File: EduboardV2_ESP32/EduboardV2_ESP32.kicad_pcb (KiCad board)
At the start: 4 copper layers, 30 x 50.9 mm, 82 parts, among them J1 EduboardV2 PCIE UP Board Conn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, Q1 S8050_C139514, Q2 S8050_C139514, Q3 AO3401A, SW1 K2-1102SP-C4SC-04, SW2 K2-1102SP-C4SC-04, U1 ESP32-WROOM-E, U2 FT2232HL, U3 M93C46-WMN6TP, U4 SX1509BIULTRT, U5 LD1117S33TR_SOT223, Y2 12MHz

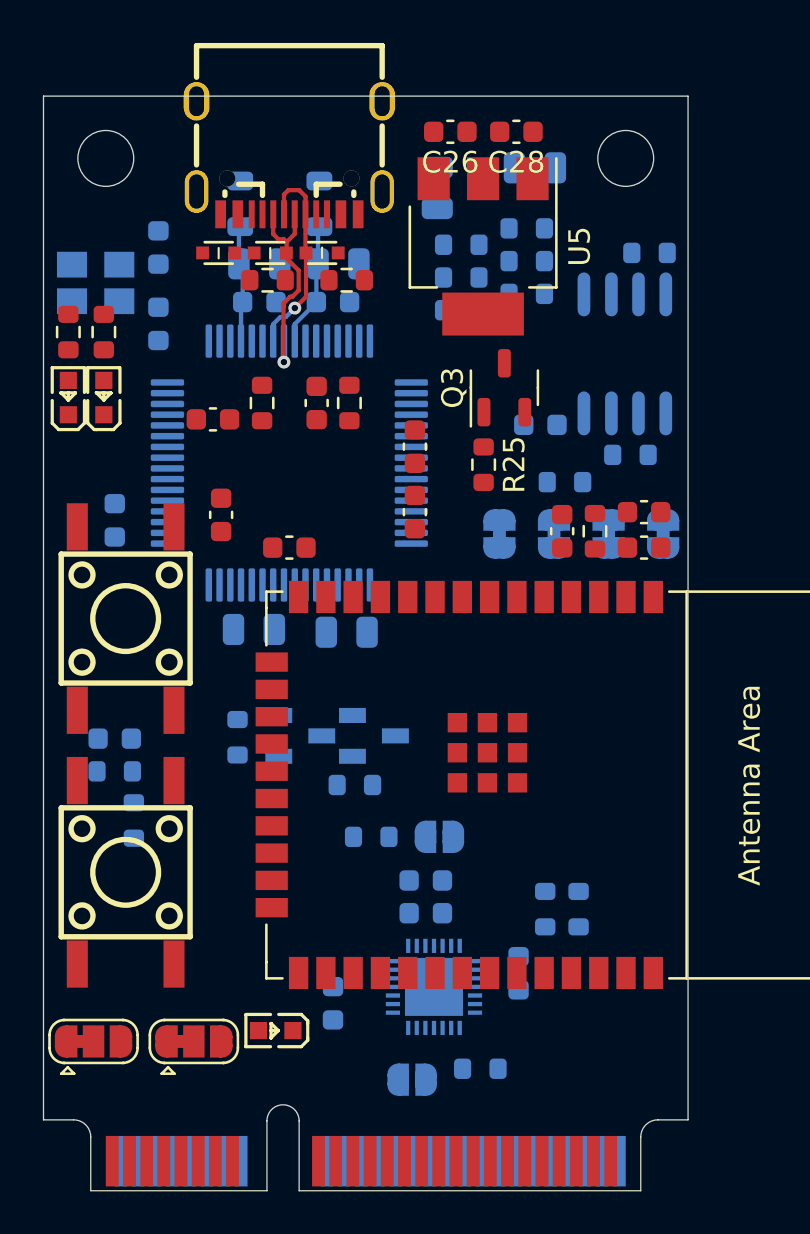
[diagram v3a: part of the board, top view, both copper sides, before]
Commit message: rework pin assignement with esp32 pin restrictions in mind. start layout
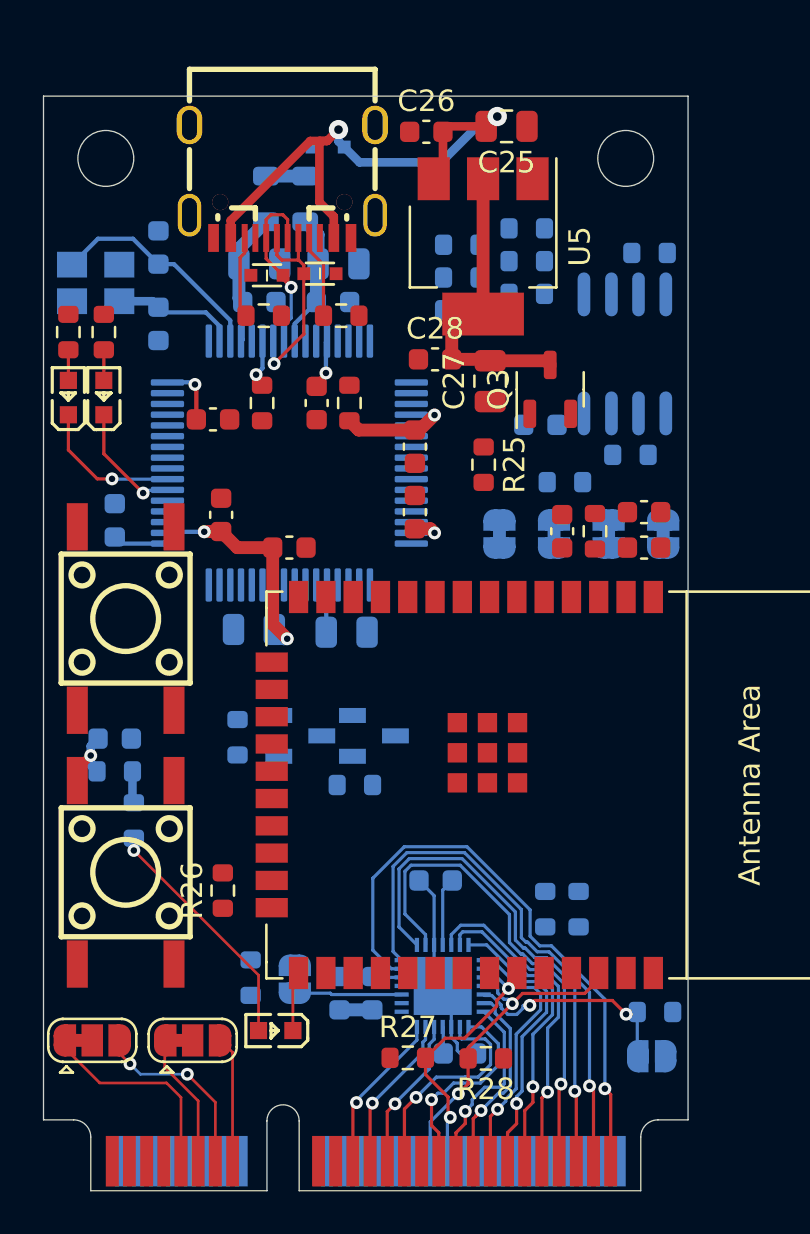
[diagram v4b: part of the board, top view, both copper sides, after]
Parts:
- added R26: 10k, Resistor_SMD:R_0603_1608Metric, F.Cu at (112.7, 143.5)
- added R27: 10k, Resistor_SMD:R_0603_1608Metric, F.Cu at (121.3, 151.3)
- added R28: 10k, Resistor_SMD:R_0603_1608Metric, F.Cu at (125.0, 151.3)
- C25, C27: moved to F.Cu
- D1: moved to B.Cu
- moved C28 11.2 mm to (122.6, 118.7), turned to 0 degrees
- moved JP5 11.2 mm to (132.7, 151.2), turned to 0 degrees
- moved C27 10.1 mm to (125.2, 119.8), turned to 90 degrees
- moved JP6 9.45 mm to (116.1, 147.6), turned to -90 degrees
- moved R24 8.63 mm to (114.0, 147.5), turned to 90 degrees
- moved R23 8.55 mm to (132.8, 149.1)
- moved C23 7.45 mm to (122.6, 143.0), turned to 180 degrees
- moved D1 7.09 mm to (117.6, 108.9)
- moved C21 6.60 mm to (118.2, 148.2), turned to 90 degrees
- moved JP7 4.73 mm to (106.7, 150.4)
- moved C24 4.63 mm to (123.8, 151.1), turned to 0 degrees
- moved JP8 4.61 mm to (111.3, 150.4)
- moved C22 4.48 mm to (119.7, 148.2), turned to 90 degrees
- moved C25 4.32 mm to (125.9, 107.9), turned to 180 degrees
- moved Q3 2.13 mm to (128.0, 120.1)
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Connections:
- J1 pad 16: GPIO_RS485_DE -> ESP_TDI
- J1 pad 17: ESP_TMS -> ESP_IO27
- J1 pad 19: ESP_TDI -> ESP_TMS
- J1 pad 21: ESP_TCK -> GPIO_RotEnc_B
- J1 pad 23: ESP_TDO -> GPIO_RotEnc_A
- J1 pad 27: ESP_IO33 -> GPIO_Buzzer
- J1 pad 29: ESP_IO27 -> ESP_IO33
- J1 pad 50: GPIO_SW2 -> ESP_TDO
- J1 pad 52: GPIO_SW3 -> ESP_TCK
- U4 pad 1: GPIO_SW2 -> GPIO_PWM_R
- U4 pad 13: GPIO_LED0 -> GPIO_LED7
- U4 pad 14: GPIO_LED1 -> GPIO_LED6
- U4 pad 15: GPIO_LED2 -> GPIO_LED5
- U4 pad 16: GPIO_LED3 -> GPIO_LED4
- U4 pad 19: GPIO_LED4 -> GPIO_LED3
- U4 pad 2: GPIO_SW3 -> GPIO_Buzzer
- U4 pad 20: GPIO_LED5 -> GPIO_LED2
- U4 pad 21: GPIO_LED6 -> GPIO_LED1
- U4 pad 22: GPIO_LED7 -> GPIO_LED0
- U4 pad 27: unconnected-(U4-I/O[0]-Pad27) -> GPIO_PWM_B
- U4 pad 28: unconnected-(U4-I/O[1]-Pad28) -> GPIO_PWM_G
- U4 pad 5: GPIO_PWM_R -> GPIO_RotEnc_SW
- U4 pad 6: GPIO_PWM_G -> GPIO_RotEnc_A
- U4 pad 7: GPIO_PWM_B -> GPIO_RotEnc_B
- U4 pad 8: GPIO_RotEnc_SW -> unconnected-(U4-I/O[7]-Pad8)
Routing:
- net +3V3: track 0.00 -> 30.9 mm, vias 0 -> 4
- net GPIO_LED7: track 0.00 -> 27.8 mm, vias 0 -> 1
- net VBUS: track 0.00 -> 27.1 mm, vias 0 -> 2
- net GPIO_LED6: track 0.00 -> 25.3 mm, vias 0 -> 1
- net GPIO_LED5: track 0.00 -> 23.7 mm, vias 0 -> 1
- net GPIO_LED4: track 0.00 -> 22.8 mm, vias 0 -> 1
- net ESP_IO22: track 0.00 -> 15.5 mm, vias 0 -> 2
- net GPIO_LED3: track 0.00 -> 15.3 mm, vias 0 -> 1
- net GPIO_LED2: track 0.00 -> 14.5 mm, vias 0 -> 1
- net Net-(Q3-D): track 0.00 -> 14.2 mm
- net GPIO_LED1: track 0.00 -> 13.2 mm, vias 0 -> 1
- net ESP_IO21: track 0.00 -> 12.9 mm, vias 0 -> 2
- net GPIO_LED0: track 0.00 -> 12.1 mm, vias 0 -> 1
- net Net-(LED3-A): track 0.00 -> 11.4 mm, vias 0 -> 1
- net GND: track 0.00 -> 11.1 mm
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
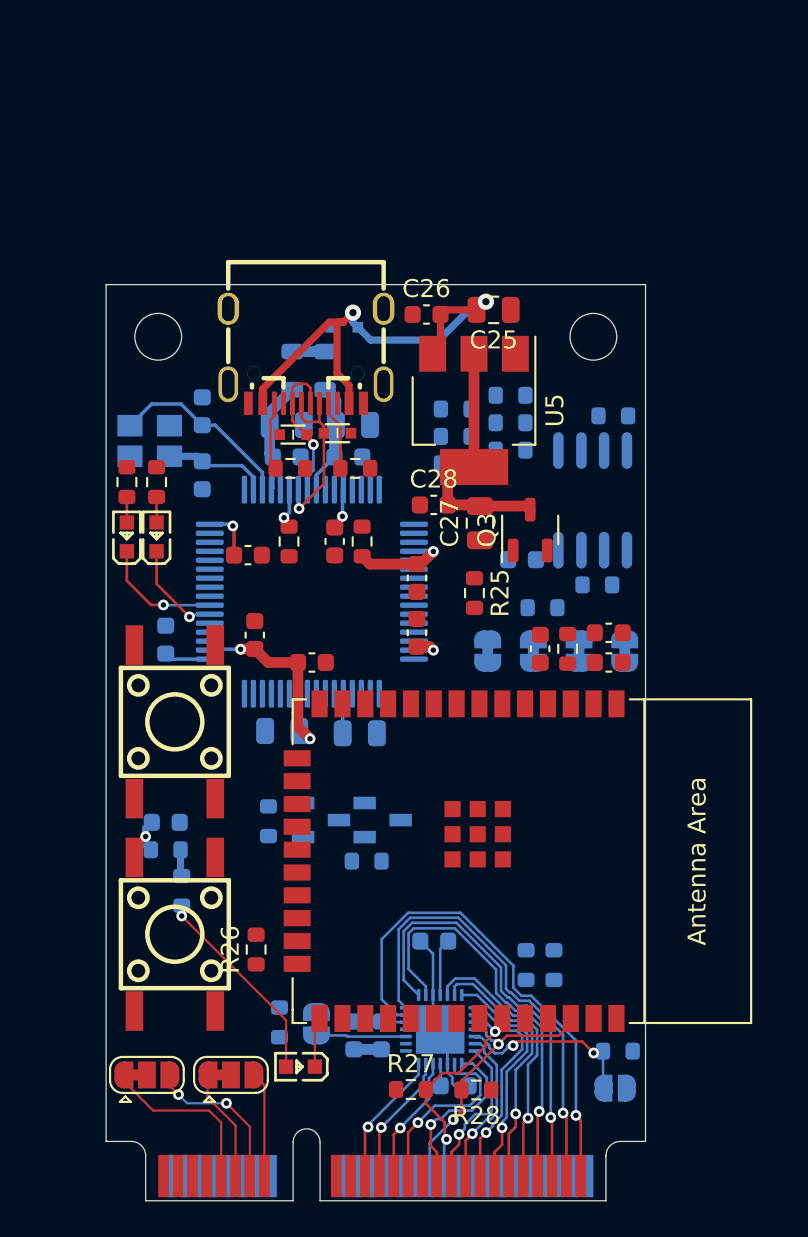
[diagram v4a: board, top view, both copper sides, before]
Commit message: resize mPCIE Board Footprint, work on ESP32 UP Board
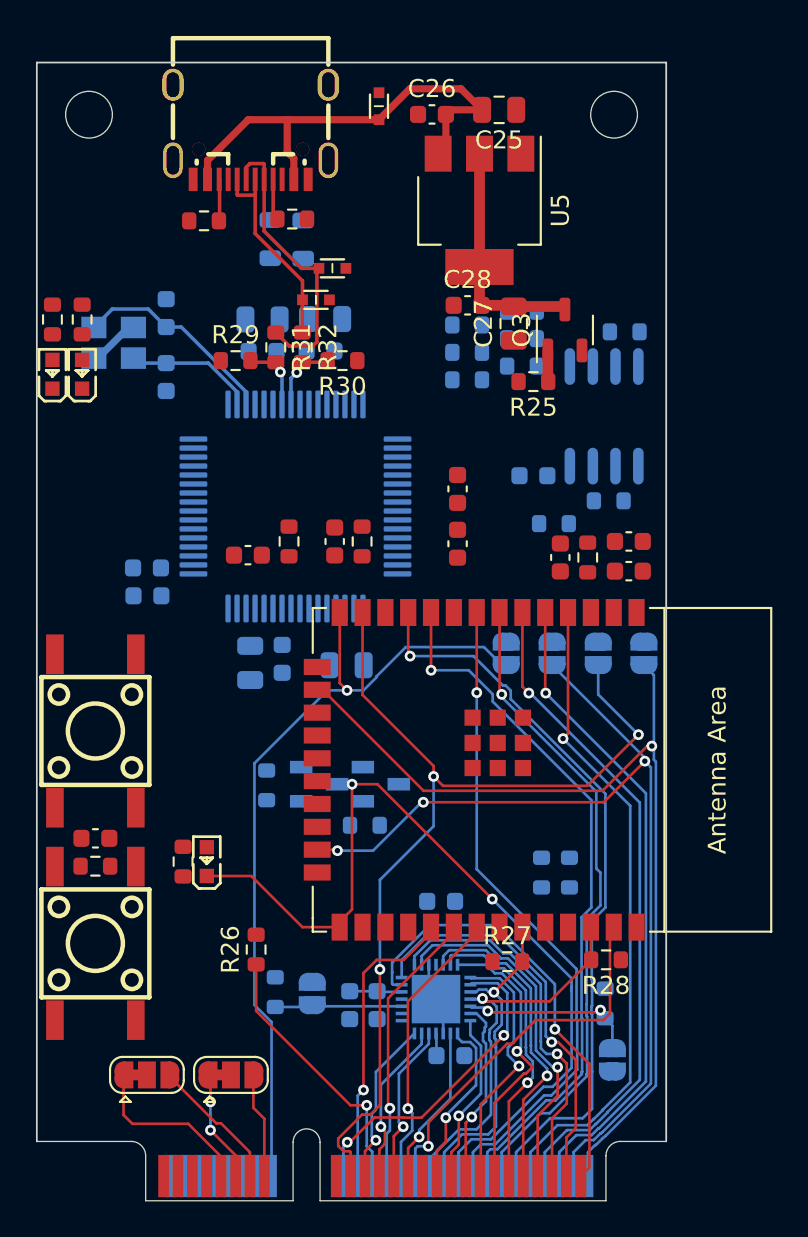
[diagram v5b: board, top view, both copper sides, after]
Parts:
- added R29: 0R, Resistor_SMD:R_0603_1608Metric, F.Cu at (111.6, 110.7)
- added R30: 0R, Resistor_SMD:R_0603_1608Metric, F.Cu at (117.5, 110.7)
- added R31: 0R, Resistor_SMD:R_0603_1608Metric, F.Cu at (113.8, 110.0)
- added R32: 0R, Resistor_SMD:R_0603_1608Metric, F.Cu at (115.3, 110.0)
- C13, C16: moved to B.Cu
- C18, D1, R20, R22: moved to F.Cu
- JP1, JP2, JP3, JP4: value SolderJumper_2_Bridged -> SolderJumper_2_Open; footprint Jumper:SolderJumper-2_P1.3mm_Bridged_RoundedPad1.0x1.5mm -> Jumper:SolderJumper-2_P1.3mm_Open_RoundedPad1.0x1.5mm
- moved R6 14.6 mm to (109.8, 102.9), turned to 180 degrees
- moved R7 14.3 mm to (114.7, 102.8)
- moved USBC1 12.8 mm to (112.4, 98.0)
- moved LED3 12.5 mm to (110.0, 138.6), turned to 90 degrees
- moved D1 12.4 mm to (119.6, 96.6), turned to -90 degrees
- moved R25 12.2 mm to (128.1, 111.9), turned to 180 degrees
- moved Q3 11.3 mm to (129.9, 109.0)
- moved C27 11.3 mm to (127.1, 108.7)
- moved C28 11.3 mm to (124.5, 107.6)
- moved U5 11.1 mm to (125.1, 102.4)
- moved C25 11.1 mm to (126.2, 96.8)
- moved C26 11.1 mm to (122.5, 97.0)
- moved R28 10.2 mm to (132.2, 144.0)
- moved LED1 9.95 mm to (103.0, 111.5)
- moved LED2 9.95 mm to (101.4, 111.5)
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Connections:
- U2 pad 7: D- -> Net-(U2-DM)
- U2 pad 8: D+ -> Net-(U2-DP)
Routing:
- net ESP_TMS: track 0.00 -> 53.5 mm, vias 0 -> 3
- net ESP_TDO: track 0.00 -> 53.1 mm, vias 0 -> 3
- net ESP_TCK: track 0.00 -> 52.3 mm, vias 0 -> 1
- net ESP_TDI: track 0.00 -> 45.0 mm, vias 0 -> 1
- net ESP_IO0: track 6.00 -> 49.1 mm, vias 1 -> 2
- net ESP_IO26: track 0.00 -> 41.2 mm, vias 0 -> 1
- net ESP_IO25: track 0.00 -> 39.2 mm, vias 0 -> 1
- net ESP_IO34: track 0.00 -> 37.0 mm, vias 0 -> 1
- net ESP_IO32: track 0.00 -> 36.8 mm, vias 0 -> 1
- net ESP_IO36: track 0.00 -> 36.3 mm, vias 0 -> 1
- net ESP_IO35: track 0.00 -> 36.3 mm, vias 0 -> 1
- net ESP_IO39: track 0.00 -> 36.2 mm, vias 0 -> 1
- net +3V3: track 30.9 -> 4.15 mm, vias 4 -> 0
- net ESP_IO23: track 0.00 -> 21.1 mm, vias 0 -> 1
- net ESP_IO4: track 0.00 -> 17.9 mm, vias 0 -> 2
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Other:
- board size 30 x 50.9 mm -> 35 x 63.3 mm

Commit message: work on layout
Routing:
- net +3V3: track 4.15 -> 139.8 mm, vias 0 -> 6
- net +1V8: track 0.00 -> 39.2 mm, vias 0 -> 3
- net ESP_IO27: track 0.00 -> 38.1 mm, vias 0 -> 2
- net Net-(U2-VPHY): track 0.00 -> 8.93 mm
- net Net-(U2-VPLL): track 0.00 -> 8.40 mm
- net GND: track 7.06 -> 14.6 mm
- net Net-(U2-~{RESET}): track 0.00 -> 7.19 mm, vias 0 -> 1
- net Net-(U2-REF): track 0.00 -> 7.18 mm, vias 0 -> 1
- net ESP_EN: track 0.00 -> 3.85 mm
- net ESP_IO2: track 15.0 -> 14.5 mm

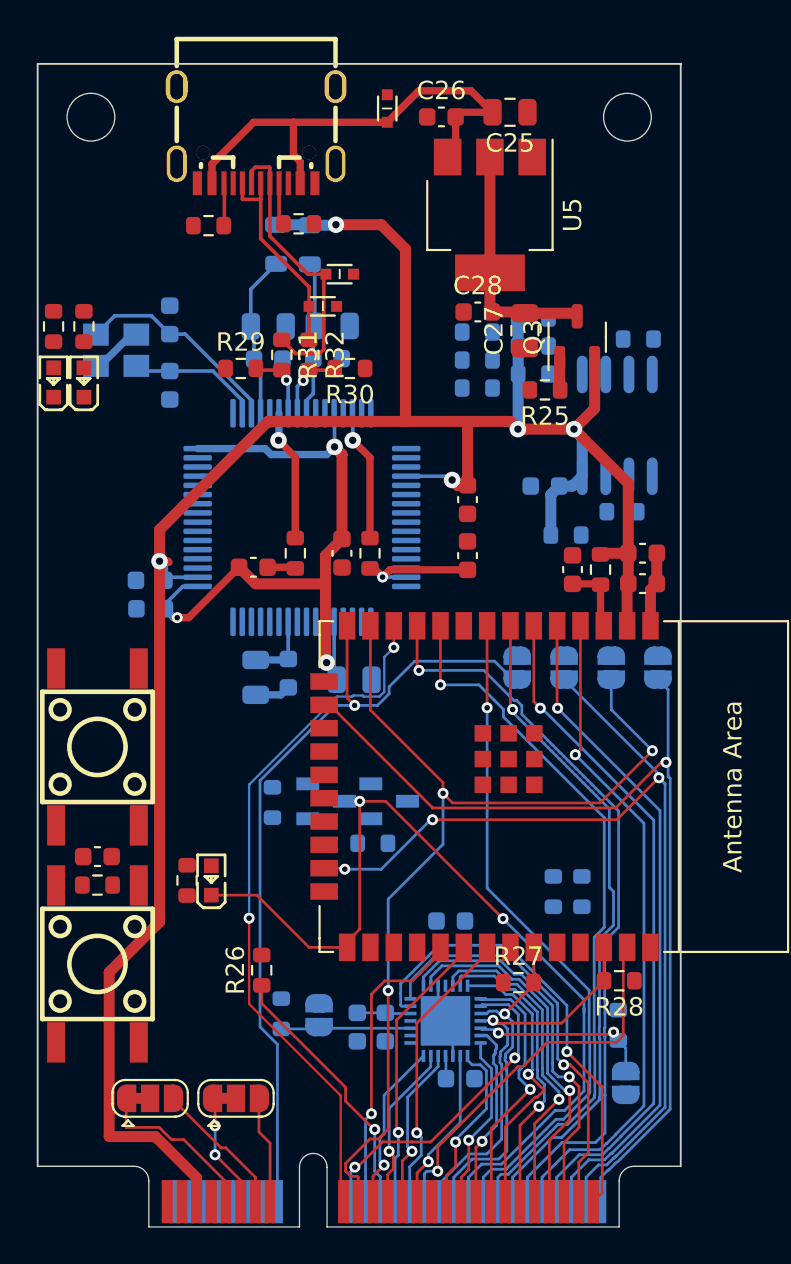
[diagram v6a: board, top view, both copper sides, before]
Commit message: layout done so far. Have to check everything and work on footprints in general. Changed to 4 layer (was not possible otherwise)
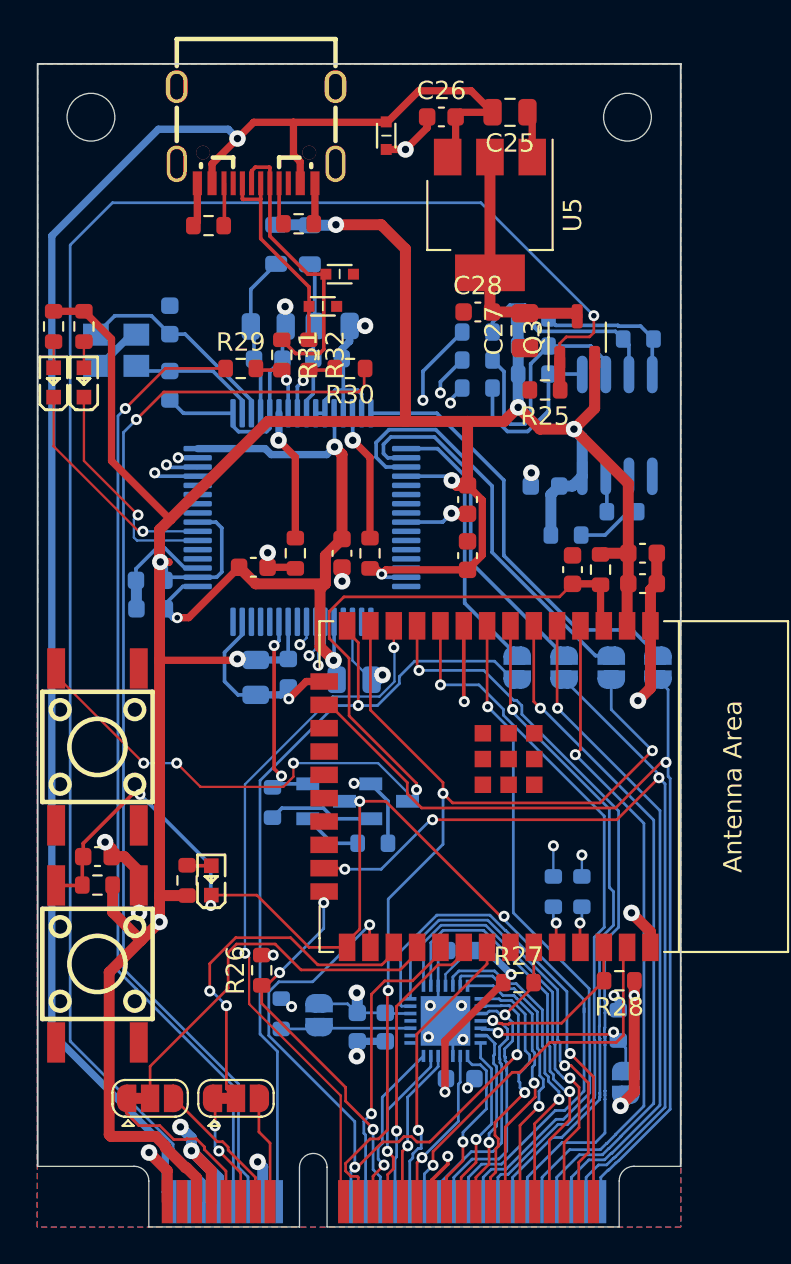
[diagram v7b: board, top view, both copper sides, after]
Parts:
- moved C23 1.71 mm to (123.6, 142.4)
- moved D1 1.48 mm to (119.5, 98.0), turned to 90 degrees
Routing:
- net GND: track 14.6 -> 111.9 mm, vias 0 -> 26
- net 3.3V_Sense: track 1.74 -> 92.6 mm, vias 0 -> 1
- net +3V3: track 139.8 -> 228.5 mm, vias 6 -> 13
- net VBUS: track 26.4 -> 94.5 mm, vias 0 -> 1
- net USB_Debug_D+: track 0.00 -> 59.8 mm, vias 0 -> 1
- net USB_Debug_D-: track 0.00 -> 52.3 mm, vias 0 -> 1
- net ESP_EN: track 3.85 -> 54.3 mm, vias 0 -> 4
- net ESP_IO33: track 0.00 -> 42.0 mm, vias 0 -> 2
- net FT_RXD: track 0.00 -> 24.6 mm, vias 0 -> 2
- net Net-(U2-EEDATA): track 0.00 -> 23.7 mm, vias 0 -> 2
- net FT_TCK: track 0.00 -> 23.5 mm
- net FT_TXD: track 0.00 -> 23.0 mm, vias 0 -> 2
- net FT_TMS: track 0.00 -> 23.0 mm
- net ESP_IO17: track 0.00 -> 21.4 mm
- net Net-(U2-EECLK): track 0.00 -> 21.0 mm, vias 0 -> 2
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- added copper zone on B.Cu, net GND
- added copper zone on F.Cu, net GND
- added copper zone on In2.Cu, net GND
